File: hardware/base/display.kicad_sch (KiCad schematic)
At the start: 2 parts, among them J4 Display

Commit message: schematic complete unreviewed
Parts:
- removed D10: PESD3V3L2UM, Package_TO_SOT_SMD:SOT-883, symbol Power_Protection:SP0502BAHT
- removed J4: Display, Connector_Molex:Molex_SlimStack_55560-0241_2x12_P0.50mm_Vertical, symbol Connector_Generic:Conn_02x12_Odd_Even
- added C26, C27: 1u, Capacitor_SMD:C_0603_1608Metric, symbol Device:C_Small
- added C28, C9: 0.1u, Capacitor_SMD:C_0402_1005Metric, symbol Device:C_Small
- added J5: Conn_01x45_Shielded, Connector_FFC-FPC:Hirose_FH12-45S-0.5SH_1x45-1MP_P0.50mm_Horizontal, symbol bt_Connector:Conn_01x45_Shielded
- added J6: CapTouch, Connector_FFC-FPC:TE_0-1734839-8_1x08-1MP_P0.5mm_Horizontal, symbol Connector_Generic_Shielded:Conn_01x08_Shielded
- added R10, R11, R12, R13, R14, R15: 100k, Resistor_SMD:R_0402_1005Metric, symbol Device:R_Small
- added R16, R17, R18, R40: 4.7k, Resistor_SMD:R_0402_1005Metric, symbol Device:R_Small
- added RN1, RN2, RN3, RN4: 100k, Resistor_SMD:R_Array_Concave_4x0402, symbol Device:R_Pack04
- added U11: AP2502, Package_TO_SOT_SMD:SOT-23-6, symbol bt_PMIC_Linear:AP2502
- added U2: 74CBTLV3257, Package_SO:TSSOP-16_4.4x5mm_P0.65mm, symbol 74xx:74CBTLV3257
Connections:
- net DISPLAY_BL: now also U11.1 (EN)
- net GND: now also C26.2, C27.2, C28.2, C9.2, J5.35 (Pin_35), J5.36 (Pin_36), J5.SH (Shield), J6.1 (Pin_1), J6.8 (Pin_8), J6.SH (Shield), R11.2, R13.2, R15.2, RN1.1 (R1.1), RN1.2 (R2.1), RN1.3 (R3.1), RN1.4 (R4.1), RN2.1 (R1.1), RN2.2 (R2.1), RN2.3 (R3.1), RN2.4 (R4.1), RN3.1 (R1.1), RN3.2 (R2.1), RN3.3 (R3.1), RN3.4 (R4.1), RN4.1 (R1.1), RN4.2 (R2.1), RN4.3 (R3.1), RN4.4 (R4.1), U11.2 (GND), U2.15 (~{OE}), U2.8 (GND)
- net SYS_I2C.SCL: now also J6.4 (Pin_4), R40.1
- net SYS_I2C.SDA: now also J6.5 (Pin_5), R18.1
- net TOUCH_INT: now also J6.6 (Pin_6), R17.1
- new net IM0: J5.1 (Pin_1), R14.2, R15.1
- new net IM1: J5.2 (Pin_2), R12.2, R13.1
- new net IM2: J5.3 (Pin_3), R10.2, R11.1
- new net LCDK1: J5.40 (Pin_40), U11.6 (LED1)
- new net LCDK2: J5.39 (Pin_39), U11.5 (LED2)
- new net LCDK3: J5.38 (Pin_38), U11.4 (LED3)
- new net LCDK4: J5.37 (Pin_37), U11.3 (LED4)
- new net LCD_CTRL.DE: J5.8 (Pin_8), RN1.8 (R1.2), U2.3
- new net LCD_CTRL.HSYNC: J5.6 (Pin_6), RN1.6 (R3.2), U2.10
- new net LCD_CTRL.PCLK: J5.7 (Pin_7), RN1.7 (R2.2), U2.6
- new net LCD_CTRL.VSYNC: J5.5 (Pin_5), RN1.5 (R4.2), U2.13
- new net LCD_MUX0: U2.4
- new net LCD_MUX1: U2.7
- new net LCD_MUX2: U2.9
- new net LCD_MUX3: U2.12
- new net LCD_RGB.B0: J5.10 (Pin_10), J5.12 (Pin_12), J5.14 (Pin_14), RN2.6 (R3.2)
- new net LCD_RGB.B1: J5.11 (Pin_11), J5.13 (Pin_13), J5.9 (Pin_9), RN2.5 (R4.2)
- new net LCD_RGB.G0: J5.17 (Pin_17), J5.20 (Pin_20), RN3.5 (R4.2)
- new net LCD_RGB.G1: J5.16 (Pin_16), J5.19 (Pin_19), RN2.8 (R1.2)
- new net LCD_RGB.G2: J5.15 (Pin_15), J5.18 (Pin_18), RN2.7 (R2.2)
- new net LCD_RGB.R0: J5.23 (Pin_23), J5.26 (Pin_26), RN3.8 (R1.2)
- new net LCD_RGB.R1: J5.22 (Pin_22), J5.25 (Pin_25), RN3.7 (R2.2)
- new net LCD_RGB.R2: J5.21 (Pin_21), J5.24 (Pin_24), RN3.6 (R3.2)
- new net LCD_SPI.DC: J5.31 (Pin_31), RN4.8 (R1.2), U2.2
- new net LCD_SPI.MISO: J5.27 (Pin_27), RN4.5 (R4.2), U2.14
- new net LCD_SPI.MOSI: J5.28 (Pin_28), RN4.6 (R3.2), U2.11
- new net LCD_SPI.SCLK: J5.30 (Pin_30), RN4.7 (R2.2), U2.5
- new net LCD_SPI_CS: J5.32 (Pin_32), U2.1 (S)
- new net RD: J5.29 (Pin_29)
- new net VDD_AUX_3V3: C26.1, C28.1, C9.1, J5.33 (Pin_33), J5.34 (Pin_34), J6.2 (Pin_2), J6.3 (Pin_3), R10.1, R12.1, R14.1, R16.2, R17.2, R18.2, R40.2, U2.16 (VCC)
- new net VDD_NVDC: C27.1, J5.41 (Pin_41)
- new net ~{RESET}: J5.4 (Pin_4), J6.7 (Pin_7), R16.1
- no-connect marks 0 -> 4

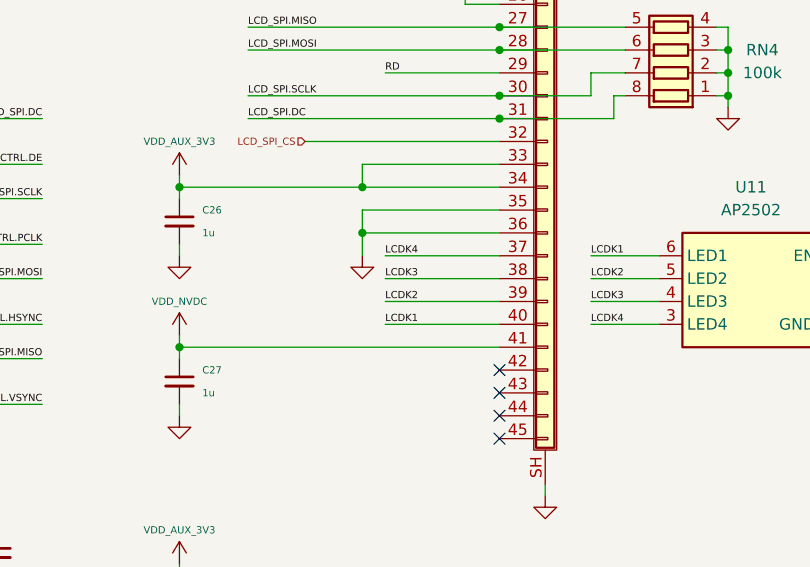
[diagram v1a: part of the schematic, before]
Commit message: Testing condensed layout
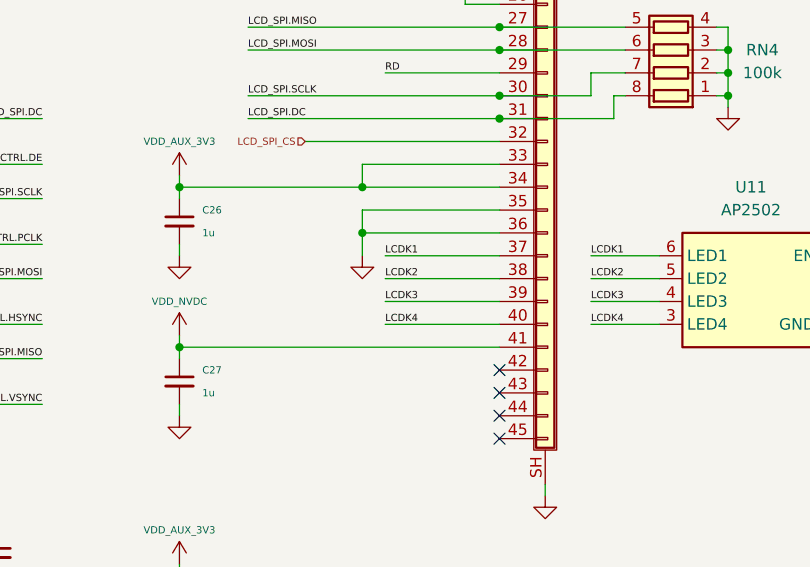
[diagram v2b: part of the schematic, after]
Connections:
- net LCDK1: now also J5.37 (Pin_37); no longer J5.40 (Pin_40)
- net LCDK2: now also J5.38 (Pin_38); no longer J5.39 (Pin_39)
- net LCDK3: now also J5.39 (Pin_39); no longer J5.38 (Pin_38)
- net LCDK4: now also J5.40 (Pin_40); no longer J5.37 (Pin_37)
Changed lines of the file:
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@@
     (stroke (width 0) (type default) (color 0 0 0 0))
   )
-  (label "LCDK3" (at 113.03 149.86 0)
+  (label "LCDK3" (at 113.03 152.4 0)
     (effects (font (size 0.8 0.8)) (justify left bottom))
   )
@@
     (effects (font (size 0.8 0.8)) (justify left bottom))
   )
-  (label "LCDK2" (at 113.03 152.4 0)
+  (label "LCDK2" (at 113.03 149.86 0)
     (effects (font (size 0.8 0.8)) (justify left bottom))
   )
@@
     (effects (font (size 0.8 0.8)) (justify left bottom))
   )
-  (label "LCDK4" (at 113.03 147.32 0)
+  (label "LCDK4" (at 113.03 154.94 0)
     (effects (font (size 0.8 0.8)) (justify left bottom))
   )
@@
     (effects (font (size 0.8 0.8)) (justify left bottom))
   )
-  (label "LCDK1" (at 113.03 154.94 0)
+  (label "LCDK1" (at 113.03 147.32 0)
     (effects (font (size 0.8 0.8)) (justify left bottom))
   )

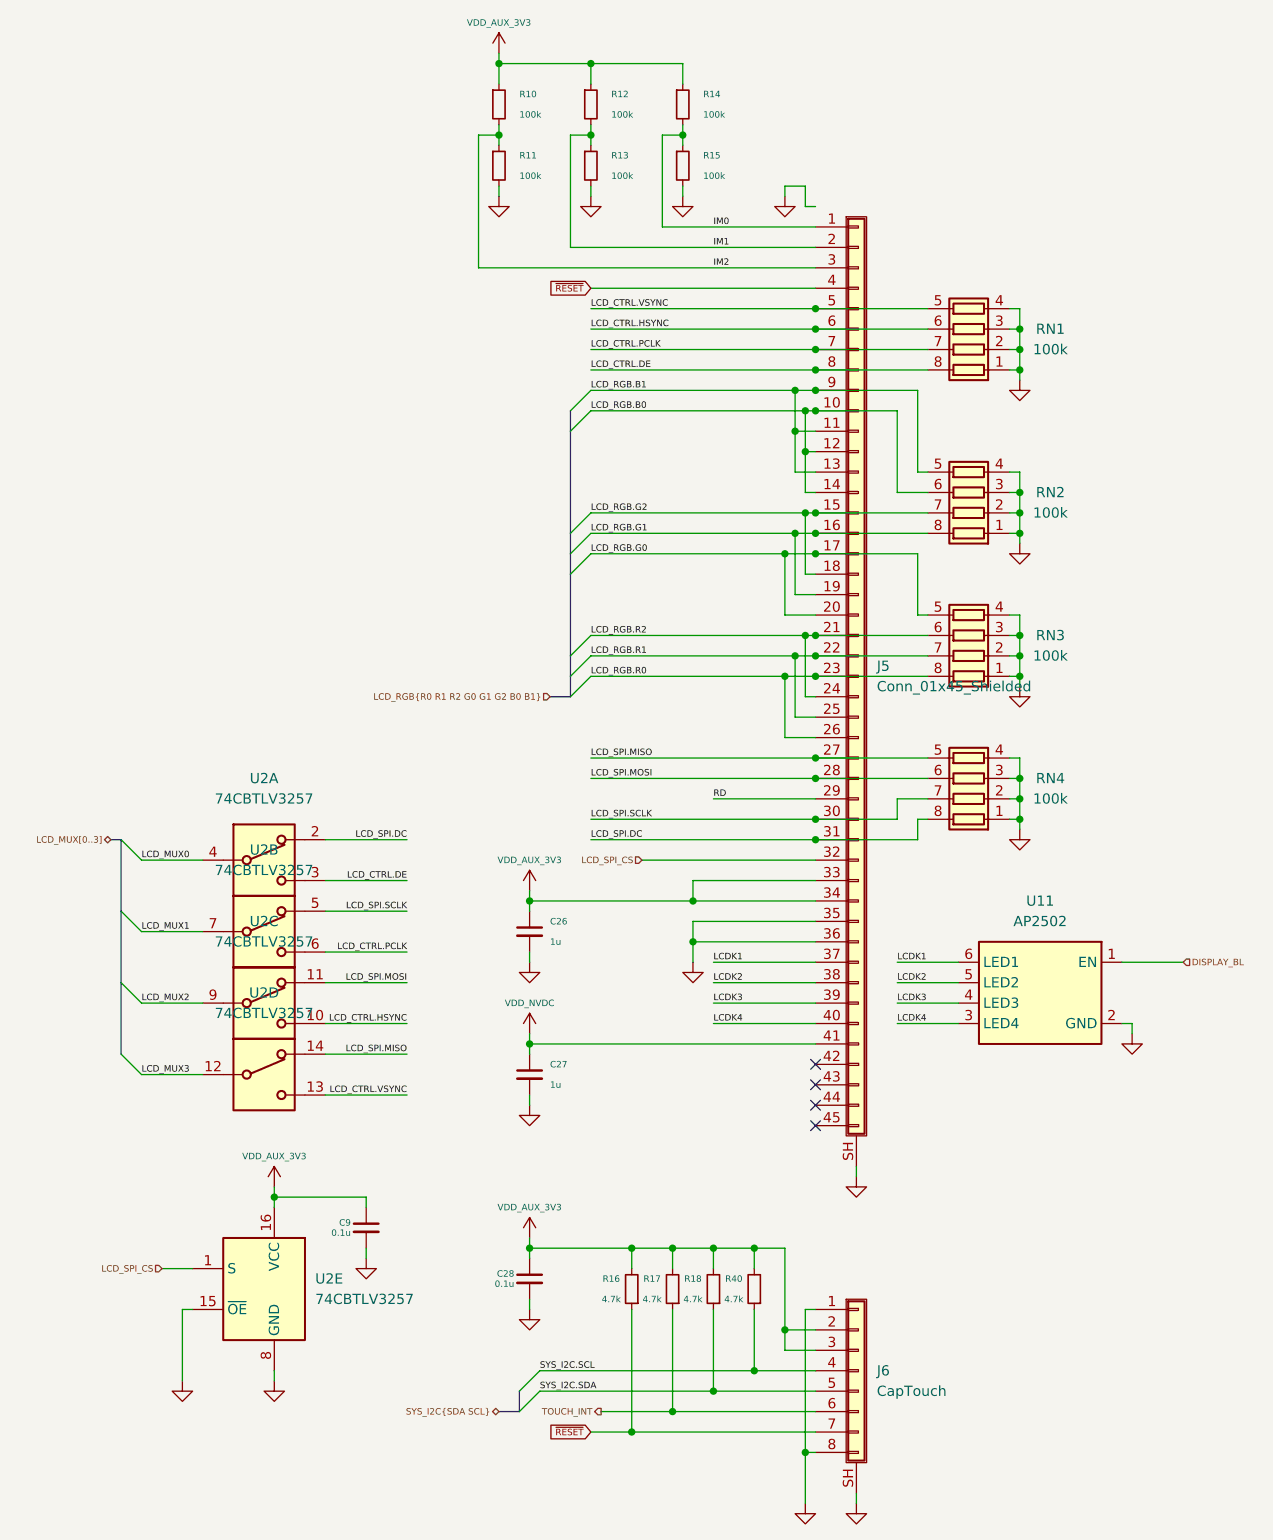
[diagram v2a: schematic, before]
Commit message: split back out condensed board into lcdboard and base
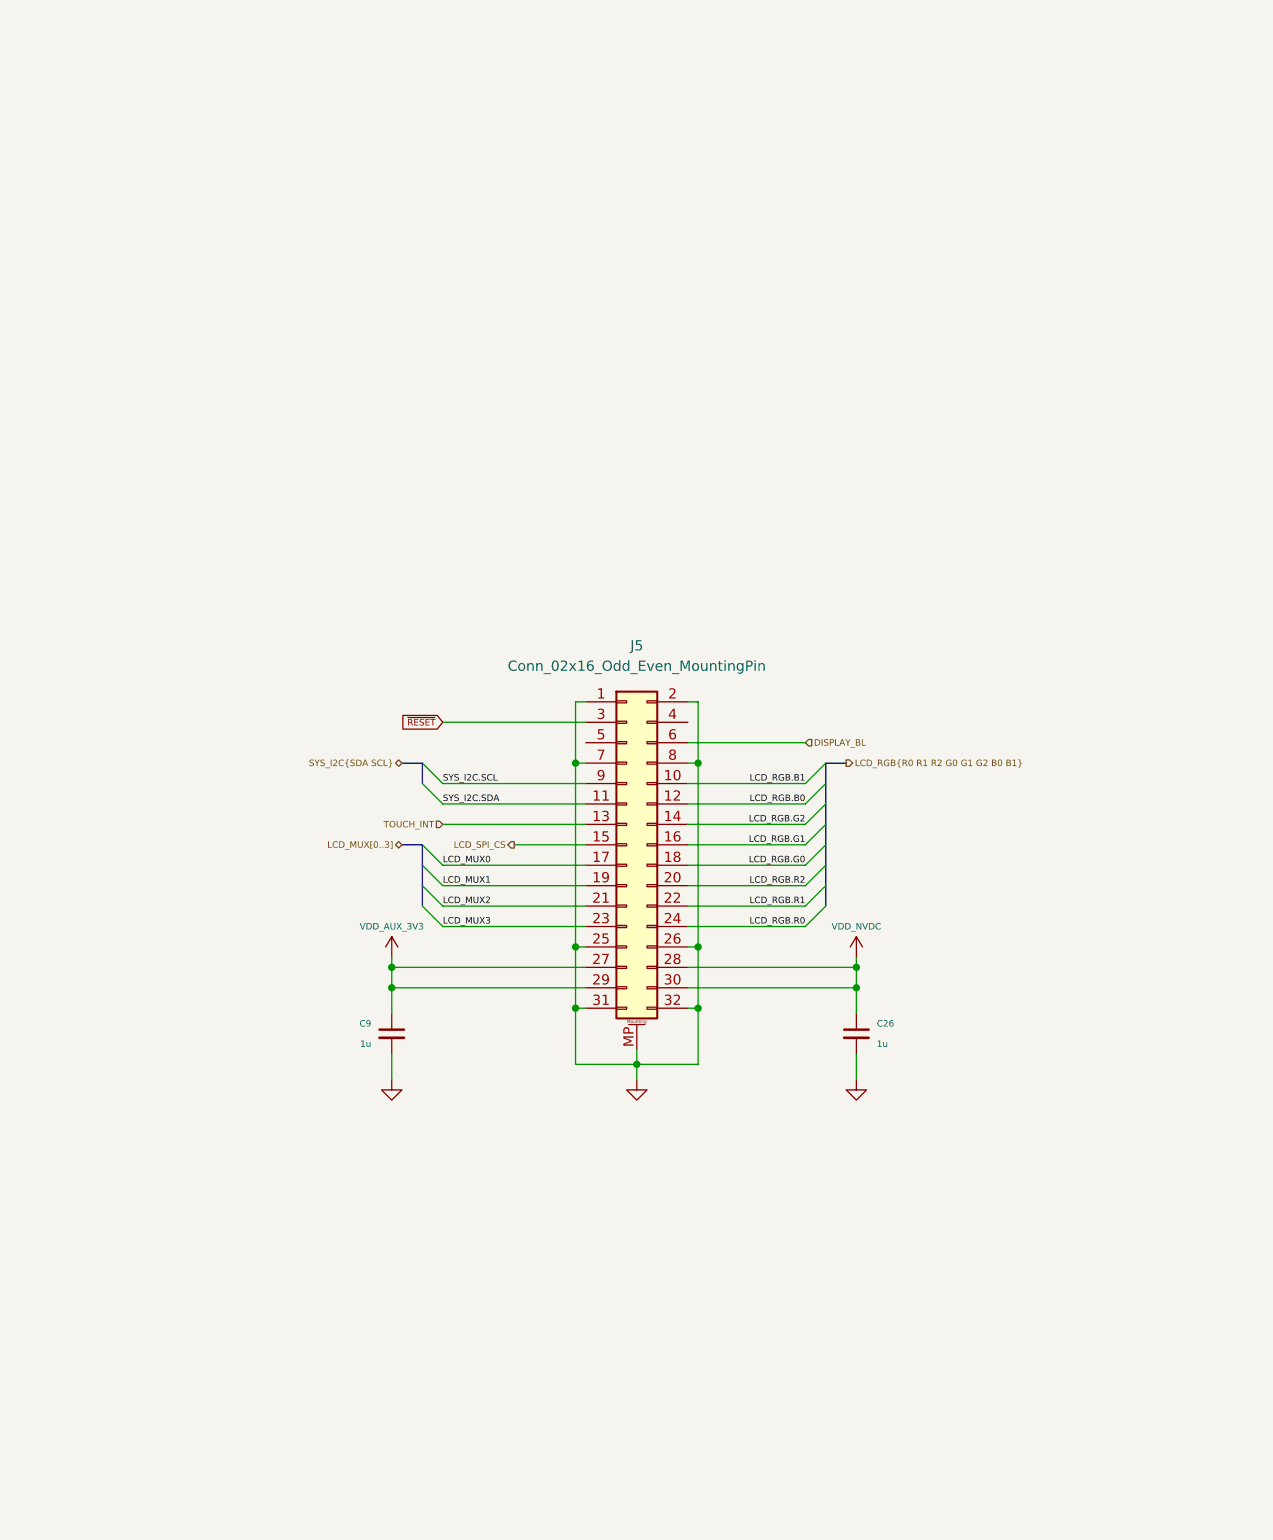
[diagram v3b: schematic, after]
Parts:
- removed C27: 1u, Capacitor_SMD:C_0603_1608Metric, symbol Device:C_Small
- removed C28: 0.1u, Capacitor_SMD:C_0402_1005Metric, symbol Device:C_Small
- removed J5: Conn_01x45_Shielded, Connector_FFC-FPC:Hirose_FH12-45S-0.5SH_1x45-1MP_P0.50mm_Horizontal, symbol bt_Connector:Conn_01x45_Shielded
- removed J6: CapTouch, Connector_FFC-FPC:TE_0-1734839-8_1x08-1MP_P0.5mm_Horizontal, symbol Connector_Generic_Shielded:Conn_01x08_Shielded
- removed R10, R11, R12, R13, R14, R15: 100k, Resistor_SMD:R_0402_1005Metric, symbol Device:R_Small
- removed R16, R17, R18, R40: 4.7k, Resistor_SMD:R_0402_1005Metric, symbol Device:R_Small
- removed RN1, RN2, RN3, RN4: 100k, Resistor_SMD:R_Array_Concave_4x0402, symbol Device:R_Pack04
- removed U11: AP2502, Package_TO_SOT_SMD:SOT-23-6, symbol bt_PMIC_Linear:AP2502
- removed U2: 74CBTLV3257, Package_SO:TSSOP-16_4.4x5mm_P0.65mm, symbol 74xx:74CBTLV3257
- added J5: Conn_02x16_Odd_Even_MountingPin, Connector_Molex:Molex_SlimStack_502426-3210_2x16_P0.40mm_Vertical, symbol Connector_Generic_MountingPin:Conn_02x16_Odd_Even_MountingPin
- C9: value 0.1u -> 1u; footprint Capacitor_SMD:C_0402_1005Metric -> Capacitor_SMD:C_0603_1608Metric
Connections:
- net DISPLAY_BL: now also J5.6 (Pin_6)
- net GND: now also J5.1 (Pin_1), J5.2 (Pin_2), J5.25 (Pin_25), J5.26 (Pin_26), J5.31 (Pin_31), J5.32 (Pin_32), J5.7 (Pin_7), J5.8 (Pin_8), J5.MP (MountPin)
- net LCD_MUX0: now also J5.17 (Pin_17)
- net LCD_MUX1: now also J5.19 (Pin_19)
- net LCD_MUX2: now also J5.21 (Pin_21)
- net LCD_MUX3: now also J5.23 (Pin_23)
- net LCD_RGB.B0: now also J5.12 (Pin_12)
- net LCD_RGB.B1: now also J5.10 (Pin_10)
- net LCD_RGB.G0: now also J5.18 (Pin_18)
- net LCD_RGB.G1: now also J5.16 (Pin_16)
- net LCD_RGB.G2: now also J5.14 (Pin_14)
- net LCD_RGB.R0: now also J5.24 (Pin_24)
- net LCD_RGB.R1: now also J5.22 (Pin_22)
- net LCD_RGB.R2: now also J5.20 (Pin_20)
- net LCD_SPI_CS: now also J5.15 (Pin_15)
- net SYS_I2C.SCL: now also J5.9 (Pin_9)
- net SYS_I2C.SDA: now also J5.11 (Pin_11)
- net TOUCH_INT: now also J5.13 (Pin_13)
- net VDD_AUX_3V3: now also J5.27 (Pin_27), J5.29 (Pin_29); no longer C26.1
- net VDD_NVDC: now also C26.1, J5.28 (Pin_28), J5.30 (Pin_30)
- net ~{RESET}: now also J5.3 (Pin_3)
- no-connect marks 4 -> 0

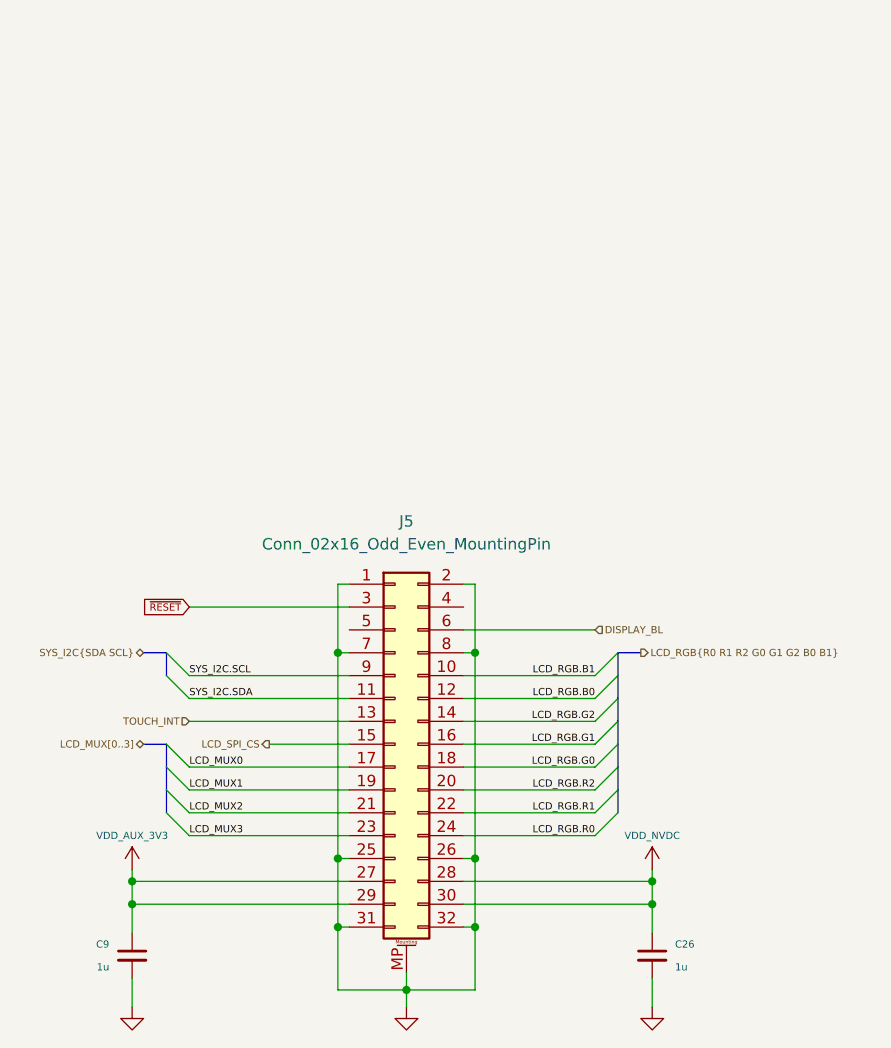
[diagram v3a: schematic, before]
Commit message: completed layout for lcdboard prototype, may need to move b2b down for clearance on mainboard.
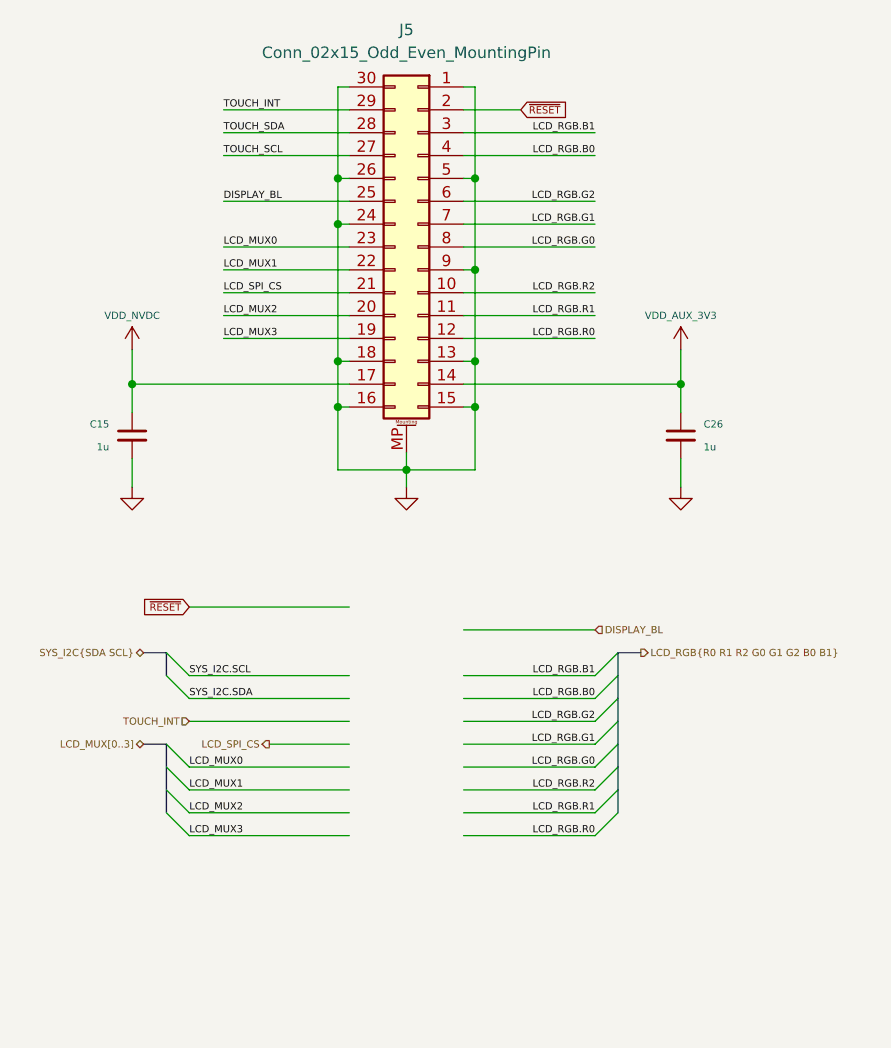
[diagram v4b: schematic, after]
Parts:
- removed C9: 1u, Capacitor_SMD:C_0603_1608Metric, symbol Device:C_Small
- removed J5: Conn_02x16_Odd_Even_MountingPin, Connector_Molex:Molex_SlimStack_502426-3210_2x16_P0.40mm_Vertical, symbol Connector_Generic_MountingPin:Conn_02x16_Odd_Even_MountingPin
- added C15: 1u, Capacitor_SMD:C_0603_1608Metric, symbol Device:C_Small
- added J5: Conn_02x15_Odd_Even_MountingPin, bt_Connector_B2B:10132797-031100LF, symbol Connector_Generic_MountingPin:Conn_02x15_Counter_Clockwise_MountingPin
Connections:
- net DISPLAY_BL: now also J5.25 (Pin_25)
- net GND: now also C15.2, J5.1 (Pin_1), J5.13 (Pin_13), J5.15 (Pin_15), J5.16 (Pin_16), J5.18 (Pin_18), J5.24 (Pin_24), J5.26 (Pin_26), J5.30 (Pin_30), J5.5 (Pin_5), J5.9 (Pin_9), J5.MP (MountPin)
- net LCD_MUX0: now also J5.23 (Pin_23)
- net LCD_MUX1: now also J5.22 (Pin_22)
- net LCD_MUX2: now also J5.20 (Pin_20)
- net LCD_MUX3: now also J5.19 (Pin_19)
- net LCD_RGB.B0: now also J5.4 (Pin_4)
- net LCD_RGB.B1: now also J5.3 (Pin_3)
- net LCD_RGB.G0: now also J5.8 (Pin_8)
- net LCD_RGB.G1: now also J5.7 (Pin_7)
- net LCD_RGB.G2: now also J5.6 (Pin_6)
- net LCD_RGB.R0: now also J5.12 (Pin_12)
- net LCD_RGB.R1: now also J5.11 (Pin_11)
- net LCD_RGB.R2: now also J5.10 (Pin_10)
- net LCD_SPI_CS: now also J5.21 (Pin_21)
- net TOUCH_INT: now also J5.29 (Pin_29)
- net VDD_AUX_3V3: now also C26.1, J5.14 (Pin_14)
- net VDD_NVDC: now also C15.1, J5.17 (Pin_17); no longer C26.1
- net ~{RESET}: now also J5.2 (Pin_2)
- new net TOUCH_SCL: J5.27 (Pin_27)
- new net TOUCH_SDA: J5.28 (Pin_28)
